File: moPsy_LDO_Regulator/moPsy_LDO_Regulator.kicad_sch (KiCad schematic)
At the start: 31 parts, among them J1 Conn_01x01_Pin, J2 Conn_01x01_Pin, J3 Conn_01x01_Pin, J4 Conn_01x01_Pin, J6 Conn_02x05_Odd_Even, Q1 TIP142, Q2 2N3904, U1 TL062, U2 LTV-827M, U3 TL062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

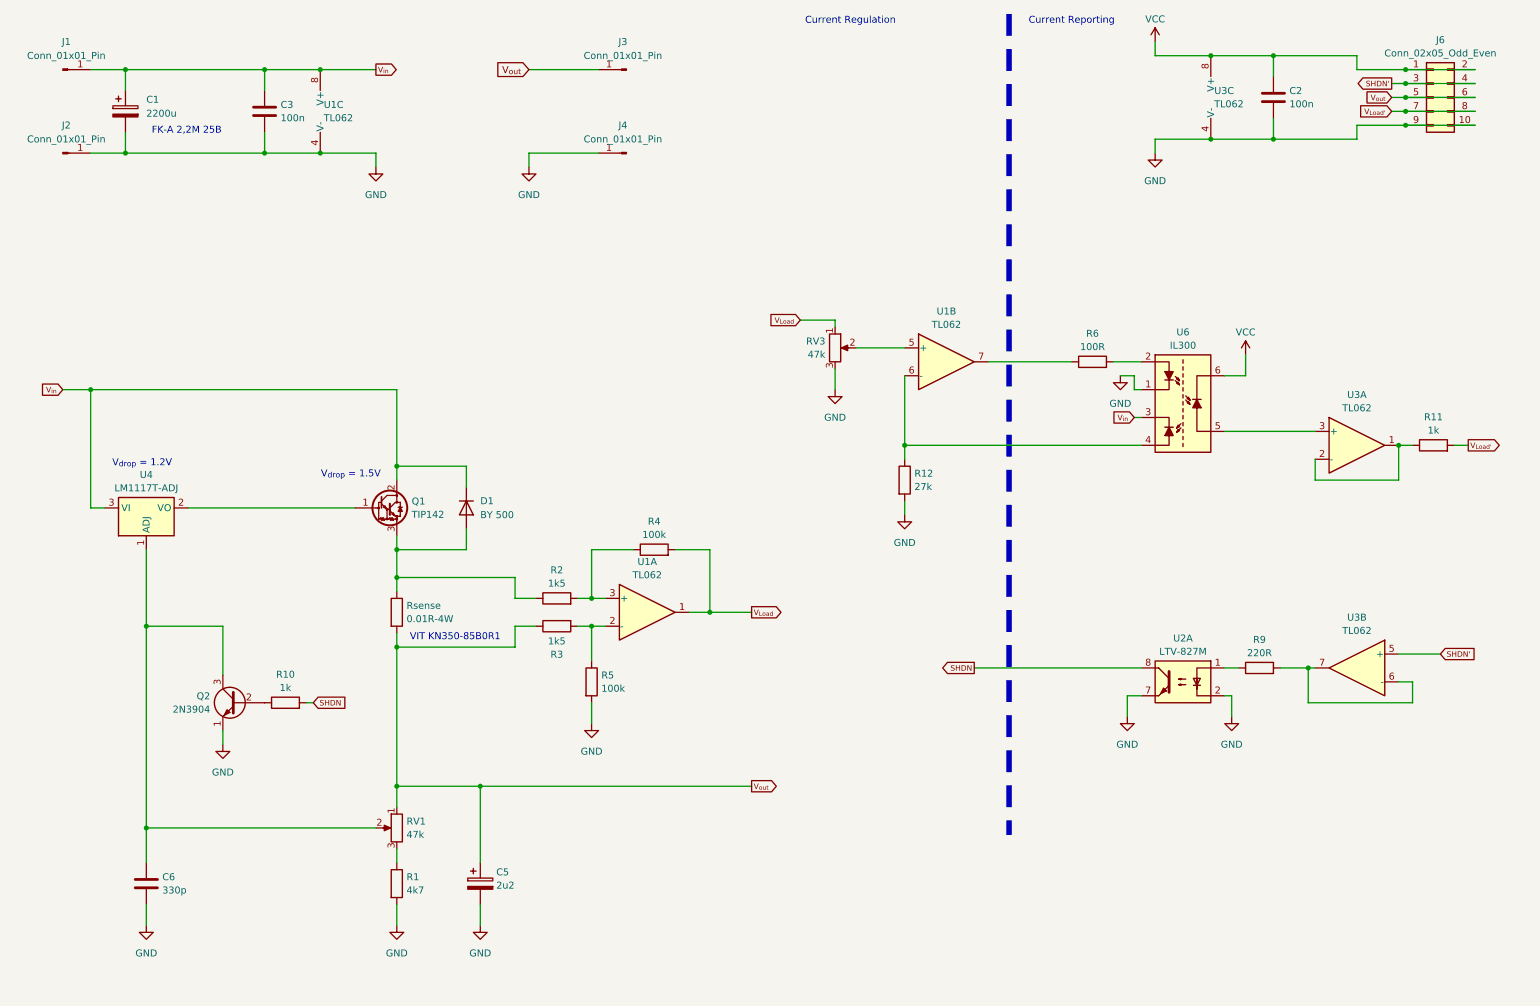
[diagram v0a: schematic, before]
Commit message: Improve based on the Jung Super Regulator
see https://tangentsoft.com/elec/opamp-linreg.html
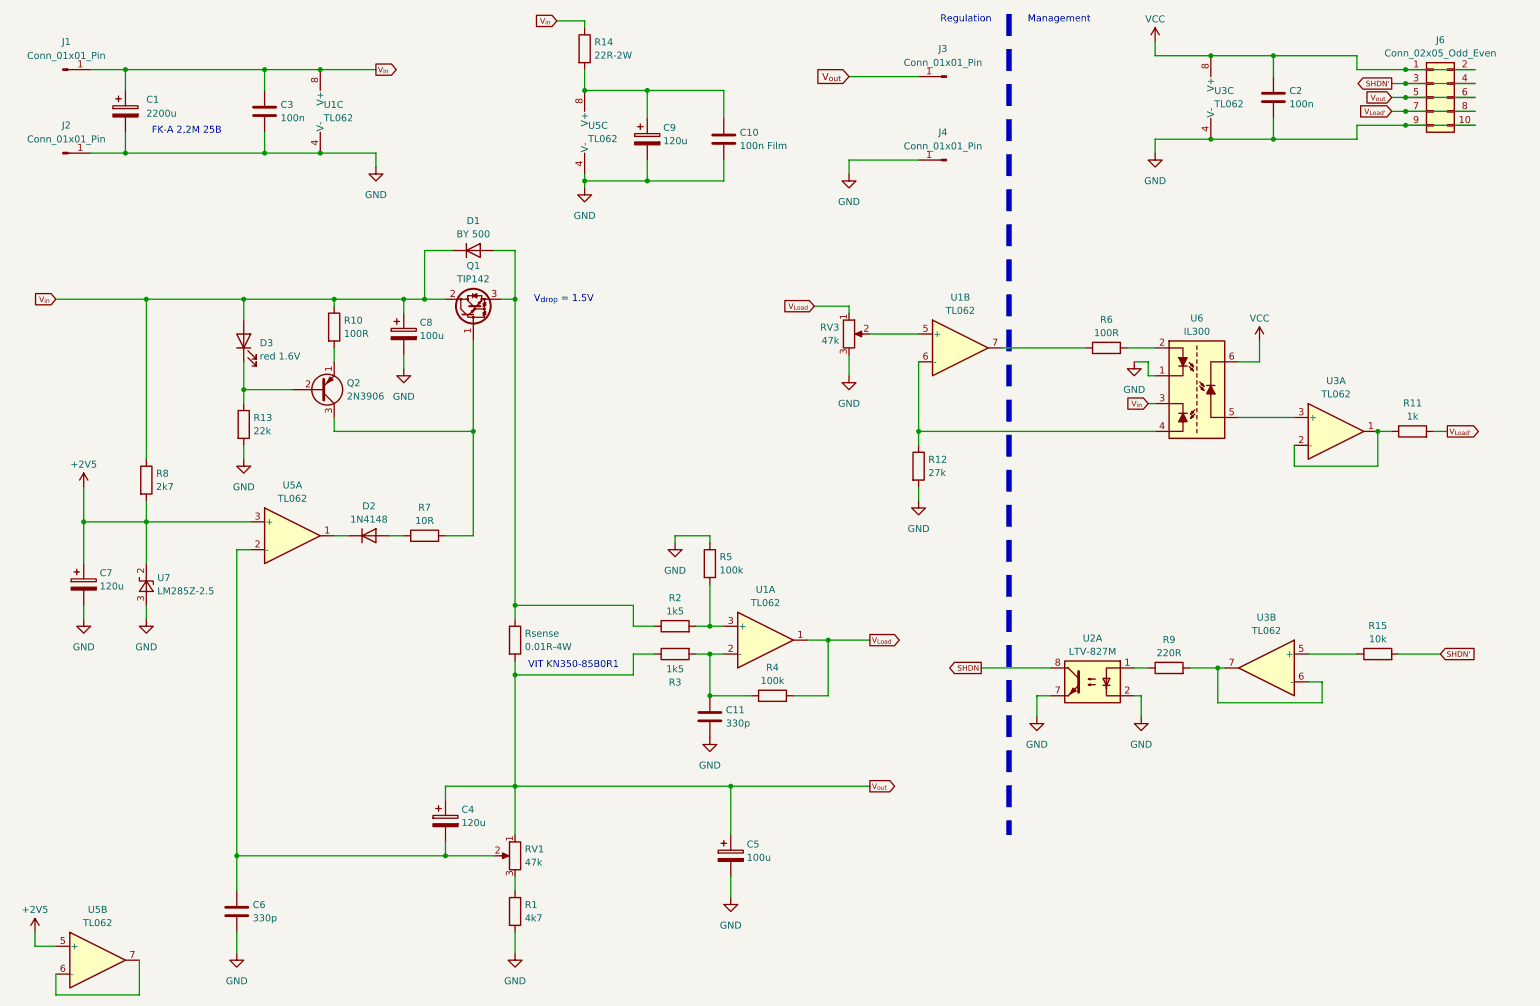
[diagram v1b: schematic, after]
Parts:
- removed Q2: 2N3904, Package_TO_SOT_THT:TO-92_Inline, symbol Transistor_BJT:2N3904
- removed U4: LM1117T-ADJ, Package_TO_SOT_THT:TO-220-3_Horizontal_TabDown, symbol Regulator_Linear:LM1117T-ADJ
- added C10: 100n Film, symbol Device:C
- added C11: 330p, symbol Device:C
- added C4, C7: 120u, symbol Device:C_Polarized
- added C8: 100u, symbol Device:C_Polarized
- added C9: 120u, Capacitor_THT:CP_Radial_D16.0mm_P7.50mm, symbol Device:C_Polarized
- added D2: 1N4148, Diode_THT:D_DO-35_SOD27_P7.62mm_Horizontal, symbol Diode:1N4148
- added D3: red 1.6V, symbol Device:LED
- added Q2: 2N3906, Package_TO_SOT_THT:TO-92_Inline, symbol Transistor_BJT:2N3906
- added R13: 22k, symbol Device:R
- added R14: 22R-2W, symbol Device:R
- added R15: 10k, symbol Device:R
- added R7: 10R, symbol Device:R
- added R8: 2k7, symbol Device:R
- added U5: TL062, symbol Amplifier_Operational:TL062
- added U7: LM285Z-2.5, Package_TO_SOT_THT:TO-92_Inline, symbol Reference_Voltage:LM285Z-2.5
- C5: value 2u2 -> 100u
- R10: value 1k -> 100R
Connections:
- net GND: now also R5.1, C10.2, C11.2, C7.2, C8.2, C9.2, R13.2, U5.4 (V-), U7.3 (A); no longer R5.2
- net SHDN: no longer R10.2
- net SHDN': now also R15.2; no longer U3.5 (+)
- net V_{in}: now also R10.1, C8.1, D3.2 (A), R14.1, R8.1
- net V_{out}: now also C4.1
- net at R2.2, U1.3 (+): now also R5.2; no longer R4.1
- net at R3.2, U1.2 (-): now also R4.1, C11.1; no longer R5.1
- net at Q1.1 (B): now also Q2.3 (C), R7.2
- net at C6.1, RV1.2: now also C4.2, U5.2 (-)
- new net: R15.1, U3.5 (+)
- new net: D3.1 (K), Q2.2 (B), R13.1
- new net: C10.1, C9.1, R14.2, U5.8 (V+)
- new net: D2.2 (A), R7.1
- new net: Q2.1 (E), R10.2
- new net: D2.1 (K), U5.1
- new net: U5.6 (-), U5.7
- new net +2V5: C7.1, R8.2, U5.3 (+), U5.5 (+), U7.2 (K)
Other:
- note added: "Management"
- note added: "Regulation"
- note removed: "Current Regulation"
- note removed: "Current Reporting"
- note removed: "V_{drop} = 1.2V"
- moved on the sheet: C5, C6, D1, J3, J4, Q1, R1, R11, R12, R2, R3, R4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
